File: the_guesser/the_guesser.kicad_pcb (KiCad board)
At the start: 4 copper layers, 24 x 75 mm, 108 parts, among them J1 Screw_Terminal_01x06, J2 Conn_Coaxial, J3 BMI-S-209-F, J4 Screw_Terminal_01x06, J5 R41-B583A, J6 BMI-S-209-F, Q1 AS2312, Q2 AS2312, Q3 AS2312, Q4 AS2312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

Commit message: Finished routing Timer Programmer
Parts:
- added R18: 10k, Resistor_SMD:R_0603_1608Metric, F.Cu at (218.0, 89.0)
- added R19: 10k, Resistor_SMD:R_0603_1608Metric, F.Cu at (218.0, 87.5)
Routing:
- net GND: track 186.5 -> 196.5 mm, vias 33 -> 34
- net SCL1: track 57.3 -> 62.8 mm
- net USB_D+: track 60.9 -> 57.7 mm
- net VCC: track 65.1 -> 68.1 mm
- net VCC_{CC1190}: track 36.0 -> 33.3 mm, vias 1 -> 2
- net SDA1: track 57.7 -> 59.7 mm
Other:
- board text added: "${REVISION}"

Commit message: Adjusted some Guesser vias
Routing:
- net SDO1: track 5.09 -> 8.56 mm
- net GND: track 196.5 -> 197.8 mm, vias 34 -> 38
- net VCC_{CC1190}: track 33.3 -> 32.8 mm

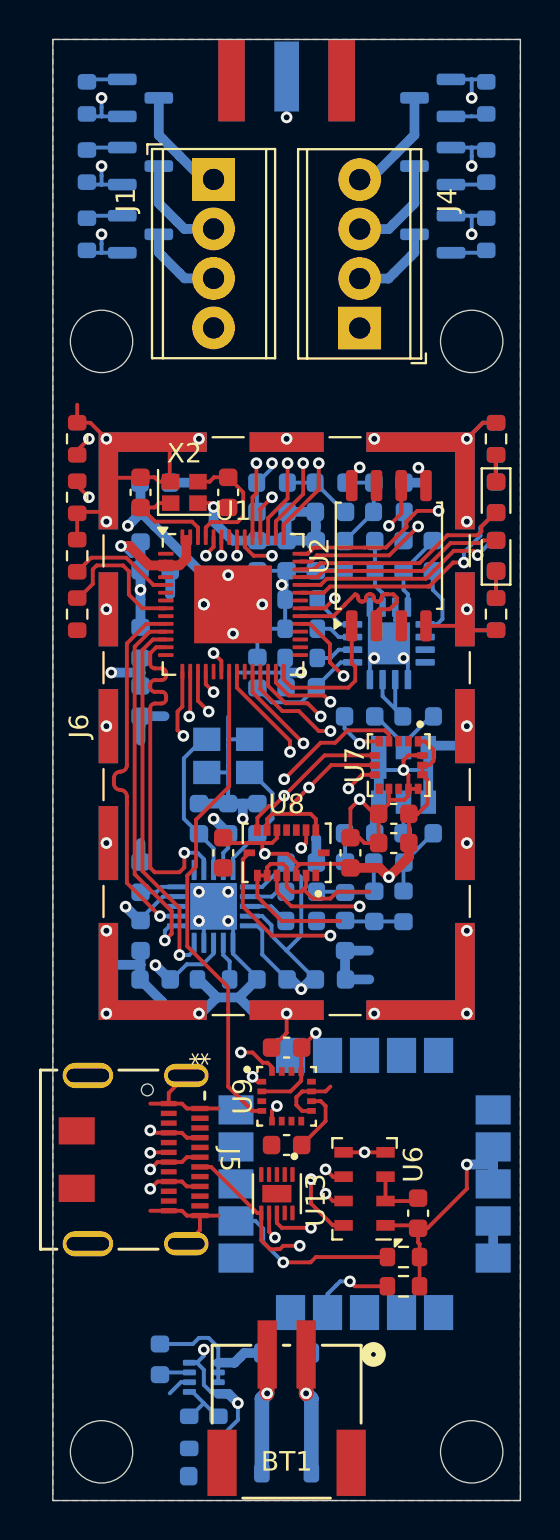
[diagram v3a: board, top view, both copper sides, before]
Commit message: Updated Guesser USB and GPS
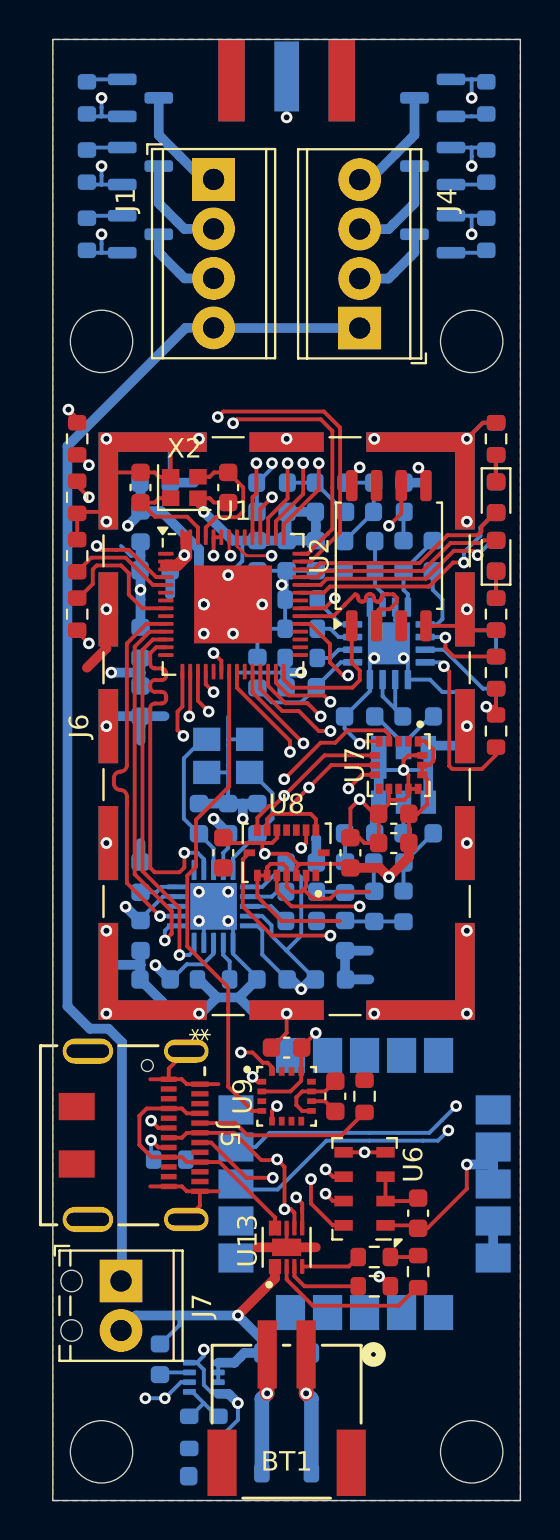
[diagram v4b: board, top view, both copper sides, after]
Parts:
- removed R18, R19: 10k, Resistor_SMD:R_0603_1608Metric
- added J7: Screw_Terminal_01x02, TerminalBlock_Phoenix:TerminalBlock_Phoenix_MPT-0,5-2-2.54_1x02_P2.54mm_Horizontal, F.Cu at (203.5, 88.7)
- added R1: 10k, Resistor_SMD:R_0603_1608Metric, F.Cu at (222.8, 60.5)
- added R20: 10k, Resistor_SMD:R_0603_1608Metric, B.Cu at (222.8, 57.5)
- added R21: 10k, Resistor_SMD:R_0603_1608Metric, F.Cu at (222.8, 57.5)
- added R22: 10k, Resistor_SMD:R_0603_1608Metric, F.Cu at (216.5, 89.0)
- added R23: 10k, Resistor_SMD:R_0603_1608Metric, F.Cu at (218.8, 88.2)
- added R24: 5.1k, Resistor_SMD:R_0603_1608Metric, F.Cu at (216.0, 79.2)
- added R25: 5.1k, Resistor_SMD:R_0603_1608Metric, B.Cu at (206.0, 82.5)
- added R28: ???, Resistor_SMD:R_0603_1608Metric, F.Cu at (216.5, 87.5)
- moved C10 3.54 mm to (214.5, 79.2), turned to -90 degrees
- moved U13 2.80 mm to (212.0, 87.0), turned to 90 degrees
- moved J5 1.25 mm to (203.6, 81.2)
- moved C13 0.25 mm to (204.5, 48.0)
- moved C14 0.25 mm to (209.0, 48.0)
- moved X2 0.25 mm to (206.8, 48.0)
- turned R13 to -90 degrees
- renumbered J2 to AE1
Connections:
- J1 pad 4: GND -> /Inputs Outputs/PYRO
- J4 pad 1: GND -> /Inputs Outputs/PYRO
- J5 pad A4: VCC -> V_{BUS}
- J5 pad A5: unconnected-(J5-CC1-PadA5) -> Net-(J5-CC1)
- J5 pad A9: VCC -> V_{BUS}
- J5 pad B4: VCC -> V_{BUS}
- J5 pad B5: unconnected-(J5-CC2-PadB5) -> Net-(J5-CC2)
- J5 pad B9: VCC -> V_{BUS}
- R11 pad 2: unconnected-(R11-Pad2) -> VCC
- R12 pad 1: Net-(U1-GPIO46) -> Net-(U1-GPIO45)
- R13 pad 1: Net-(U1-GPIO45) -> VCC
- R13 pad 2: GND -> Net-(U1-CHIP_PU)
- U1 pad 4: unconnected-(U1-CHIP_PU-Pad4) -> Net-(U1-CHIP_PU)
- U1 pad 41: SCL1 -> T_{3}
- U1 pad 42: SDA1 -> T_{2}
- U1 pad 48: T_{2} -> unconnected-(U1-MTMS-Pad48)
- U1 pad 49: T_{3} -> TXD
- U1 pad 50: unconnected-(U1-U0RXD-Pad50) -> RXD
- U1 pad 52: Net-(U1-GPIO46) -> Net-(U1-GPIO45)
- U11 pad 12: SCL1 -> unconnected-(U11-SCL-Pad12)
- U11 pad 13: unconnected-(U11-TXD-Pad13) -> TXD
- U11 pad 14: unconnected-(U11-RXD-Pad14) -> RXD
- U11 pad 9: SDA1 -> unconnected-(U11-SDA-Pad9)
- U13 pad 1: unconnected-(U13-VBUSOUT_1-Pad1) -> V_{B}
- U13 pad 10: unconnected-(U13-VBUS_10-Pad10) -> V_{BUS}
- U13 pad 11: unconnected-(U13-EXP-Pad11) -> GND
- U13 pad 2: unconnected-(U13-VBUSOUT_2-Pad2) -> V_{B}
- U13 pad 3: unconnected-(U13-~{EN}-Pad3) -> Net-(U13-~{EN})
- U13 pad 4: unconnected-(U13-~{ACK}-Pad4) -> Net-(U13-~{ACK})
- U13 pad 5: unconnected-(U13-ID-Pad5) -> USB_ID
- U13 pad 9: unconnected-(U13-VBUS_9-Pad9) -> V_{BUS}
- U4 pad 6: unconnected-(U4-HGM-Pad6) -> HGM
- U4 pad 7: unconnected-(U4-LNA-EN-Pad7) -> LNA_EN
- U4 pad 8: unconnected-(U4-PA-EN-Pad8) -> PA_EN
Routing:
- net SCL1: track 62.8 -> 0.00 mm, vias 2 -> 0
- net /Inputs Outputs/PYRO: track 0.00 -> 62.1 mm
- net SDA1: track 59.7 -> 0.00 mm, vias 2 -> 0
- net RXD: track 0.00 -> 50.5 mm, vias 0 -> 2
- net TXD: track 0.00 -> 50.0 mm, vias 0 -> 2
- net GND: track 197.8 -> 216.9 mm, vias 38 -> 40
- net V_{BUS}: track 0.00 -> 13.9 mm
- net Net-(U1-GPIO46): track 10.3 -> 0.00 mm, vias 2 -> 0
- net V_{B}: track 7.55 -> 17.4 mm, vias 0 -> 1
- net Net-(U1-CHIP_PU): track 0.00 -> 9.84 mm, vias 0 -> 2
- net PA_EN: track 0.00 -> 9.45 mm, vias 0 -> 1
- net Net-(J5-CC1): track 0.00 -> 9.20 mm
- net Net-(U13-~{EN}): track 0.00 -> 8.36 mm
- net T_{3}: track 23.1 -> 29.4 mm
- net VCC: track 68.1 -> 62.8 mm, vias 13 -> 15
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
